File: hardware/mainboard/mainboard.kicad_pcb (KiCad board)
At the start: 4 copper layers, 28 x 110 mm, 45 parts, among them J1 Power Connector, J2 IN1, J3 IN2, J4 IN3, J5 INV OUT, J6 OUT, J7 CLIP OUT, U1 TL074

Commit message: Clean up
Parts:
- moved D3 9.90 mm to (53.9, 130.8)
- moved D4 9.32 mm to (53.9, 142.2)
- moved C4 9.24 mm to (66.5, 137.4), turned to -90 degrees
- moved R2 8.64 mm to (53.9, 139.8)
- moved R1 8.55 mm to (53.9, 133.2)
- moved C3 6.18 mm to (66.5, 133.2), turned to -90 degrees
- moved C1 4.93 mm to (60.2, 131.0), turned to -90 degrees
- moved C2 4.90 mm to (60.2, 141.2), turned to -90 degrees
- moved D1 4.37 mm to (66.5, 129.0), turned to 90 degrees
- moved D2 3.98 mm to (66.5, 142.7), turned to 90 degrees
- moved R11 1.91 mm to (74.9, 154.7), turned to 0 degrees
- moved R9 1.80 mm to (53.3, 154.7), turned to 180 degrees
- moved J1 1.70 mm to (71.5, 138.5)
- moved R10 1.64 mm to (63.0, 154.7), turned to 180 degrees
- moved C5 1.36 mm to (58.9, 102.4), turned to -90 degrees
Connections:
- net Net-(D5-A) renamed CLIP_DIODES
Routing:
- net -12V: track 75.6 -> 65.1 mm, vias 3 -> 4
- net Net-(D1-A): track 14.8 -> 7.81 mm, vias 1 -> 0
- net GND: track 3.32 -> 6.08 mm, vias 13 -> 15
- net Net-(J7-PadT): track 1.86 -> 4.33 mm
- net Net-(J5-PadT): track 1.86 -> 4.26 mm
- net Net-(J6-PadT): track 1.82 -> 4.12 mm
- net OUT: track 72.4 -> 70.5 mm
- net Net-(D2-K): track 11.6 -> 9.95 mm, vias 1 -> 0
- net CLIP_OUT: track 71.3 -> 69.9 mm, vias 2 -> 1
- net +12V: track 66.4 -> 66.8 mm, vias 2 -> 4
- net INV_OUT: track 77.3 -> 77.4 mm, vias 3 -> 4

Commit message: Cleanup
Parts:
- moved C3 2.20 mm to (66.3, 131.1)
- moved C4 2.07 mm to (66.3, 135.3)
- moved D1 2.01 mm to (66.3, 127.0)
- moved D2 1.22 mm to (66.3, 141.5)
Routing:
- net +12V: track 66.8 -> 64.2 mm
- net Net-(D1-A): track 7.81 -> 8.73 mm
- net GND: vias 15 -> 13
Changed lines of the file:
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@@
 	(footprint "Diode_SMD:D_SOD-323F"
 		(layer "B.Cu")
-		(at 66.5 129 90)
+		(at 66.3 127 90)
 		(descr "SOD-323F http://www.nxp.com/documents/outline_drawing/SOD323F.pdf")
 		(tags "SOD-323F")
@@
 	(footprint "Capacitor_SMD:C_0805_2012Metric_Pad1.18x1.45mm_HandSolder"
 		(layer "B.Cu")
-		(at 66.5 133.2375 -90)
+		(at 66.3 131.05125 -90)
 		(descr "Capacitor SMD 0805 (2012 Metric), square (rectangular) end terminal, IPC-7351 nominal with elongated pad for handsoldering. (Body size source: IPC-SM-782 page 76, https://www.pcb-3d.com/wordpress/wp-content/uploads/ipc-sm-782a_amendment_1_and_2.pdf, https://docs.google.com/spreadsheets/d/1BsfQQcO9C6DZCsRaXUlFlo91Tg2WpOkGARC1WS5S8t0/edit?usp=sharing), generated with kicad-footprint-generator")
 		(tags "capacitor handsolder")
@@
 	(footprint "Diode_SMD:D_SOD-323F"
 		(layer "B.Cu")
-		(at 66.5 142.7 90)
+		(at 66.3 141.5 90)
 		(descr "SOD-323F http://www.nxp.com/documents/outline_drawing/SOD323F.pdf")
 		(tags "SOD-323F")
@@
 	(footprint "Capacitor_SMD:C_0805_2012Metric_Pad1.18x1.45mm_HandSolder"
 		(layer "B.Cu")
-		(at 66.5 137.4 -90)
+		(at 66.3 135.3375 -90)
 		(descr "Capacitor SMD 0805 (2012 Metric), square (rectangular) end terminal, IPC-7351 nominal with elongated pad for handsoldering. (Body size source: IPC-SM-782 page 76, https://www.pcb-3d.com/wordpress/wp-content/uploads/ipc-sm-782a_amendment_1_and_2.pdf, https://docs.google.com/spreadsheets/d/1BsfQQcO9C6DZCsRaXUlFlo91Tg2WpOkGARC1WS5S8t0/edit?usp=sharing), generated with kicad-footprint-generator")
 		(tags "capacitor handsolder")
@@
 	)
 	(via
-		(at 66.5 136.3625)
-		(size 0.6)
-		(drill 0.3)
-		(layers "F.Cu" "B.Cu")
-		(net 1)
-	)
-	(via
 		(at 69.6 70.2)
 		(size 0.6)
@@
 	)
 	(via
-		(at 66.5 134.275)
-		(size 0.6)
-		(drill 0.3)
-		(layers "F.Cu" "B.Cu")
-		(net 1)
-	)
-	(via
 		(at 61.5 100.54)
 		(size 0.6)
@@
 	)
 	(segment
-		(start 60.25 128.25)
-		(end 62.55 128.25)
-		(width 0.3)
+		(start 65.201 109.723)
+		(end 65.201 100.701)
+		(width 0.2)
 		(layer "F.Cu")
 		(net 2)
 	)
 	(segment
-		(start 65.201 109.723)
-		(end 65.201 100.701)
+		(start 74 113.529009)
+		(end 74 113)
 		(width 0.2)
 		(layer "F.Cu")
@@
 	)
 	(segment
-		(start 74 113)
-		(end 74 114.5)
+		(start 66.3 130.01375)
+		(end 66.3 121.229009)
 		(width 0.2)
 		(layer "F.Cu")
@@
 	)
 	(segment
-		(start 74 114.5)
-		(end 60.2 128.3)
+		(start 60.2 128.3)
+		(end 64.58625 128.3)
+		(width 0.3)
+		(layer "F.Cu")
+		(net 2)
+	)
+	(segment
+		(start 66.3 121.229009)
+		(end 74 113.529009)
 		(width 0.2)
 		(layer "F.Cu")
@@
 	)
 	(segment
-		(start 62.55 128.25)
-		(end 66.5 132.2)
+		(start 64.58625 128.3)
+		(end 66.3 130.01375)
 		(width 0.3)
 		(layer "F.Cu")
@@
 	)
 	(via
-		(at 66.5 132.2)
+		(at 52.9 130.8)
 		(size 0.6)
 		(drill 0.3)
@@
 	)
 	(via
-		(at 52.9 130.8)
+		(at 64.75 100.25)
 		(size 0.6)
 		(drill 0.3)
@@
 	)
 	(via
-		(at 64.75 100.25)
+		(at 66.3 130.01375)
 		(size 0.6)
 		(drill 0.3)
@@
 	)
 	(segment
-		(start 66.5 130.1)
-		(end 66.5 132.2)
-		(width 0.3)
+		(start 63.19 101.81)
+		(end 61.5 101.81)
+		(width 0.2)
 		(layer "B.Cu")
 		(net 2)
 	)
 	(segment
-		(start 63.19 101.81)
-		(end 61.5 101.81)
+		(start 66.5 127.9)
+		(end 66.4 127.9)
 		(width 0.2)
 		(layer "B.Cu")
@@
 	)
 	(segment
-		(start 61.5 101.81)
-		(end 59.31 101.81)
+		(start 66.3 130.01375)
+		(end 66.3 128.1)
 		(width 0.2)
 		(layer "B.Cu")
@@
 	)
 	(segment
-		(start 66.4 132.2)
-		(end 65.949 131.749)
+		(start 61.5 101.81)
+		(end 59.31 101.81)
 		(width 0.2)
 		(layer "B.Cu")
@@
 	)
 	(segment
-		(start 67.101 137.8365)
-		(end 66.5 138.4375)
-		(width 0.2)
+		(start 69 125)
+		(end 74 120)
+		(width 0.3)
 		(layer "F.Cu")
 		(net 3)
 	)
 	(segment
-		(start 74 120)
-		(end 67.101 126.899)
-		(width 0.2)
+		(start 66.3 136.375)
+		(end 69 133.675)
+		(width 0.3)
+		(layer "F.Cu")
+		(net 3)
+	)
+	(segment
+		(start 60.25 143.95)
+		(end 66.3 137.9)
+		(width 0.3)
 		(layer "F.Cu")
 		(net 3)
 	)
 	(segment
-		(start 65.7625 138.4375)
-		(end 66.5 138.4375)
+		(start 69 133.675)
+		(end 69 125)
 		(width 0.3)
 		(layer "F.Cu")
@@
 	)
 	(segment
-		(start 67.101 126.899)
-		(end 67.101 137.8365)
-		(width 0.2)
+		(start 66.3 137.9)
+		(end 66.3 136.375)
+		(width 0.3)
 		(layer "F.Cu")
 		(net 3)
@@
 		(net 3)
 	)
-	(segment
-		(start 60.25 143.95)
-		(end 65.7625 138.4375)
-		(width 0.3)
-		(layer "F.Cu")
-		(net 3)
-	)
 	(via
-		(at 66.5 138.4375)
+		(at 55 142.2)
 		(size 0.6)
 		(drill 0.3)
@@
 	)
 	(via
-		(at 55 142.2)
+		(at 60.25 143.95)
 		(size 0.6)
 		(drill 0.3)
@@
 	)
 	(via
-		(at 60.25 143.95)
+		(at 66.3 136.375)
 		(size 0.6)
 		(drill 0.3)
@@
 	)
 	(segment
-		(start 66.3 138.4375)
-		(end 65.949 138.7885)
-		(width 0.2)
-		(layer "B.Cu")
-		(net 3)
-	)
-	(segment
-		(start 66.5 141.6)
-		(end 66.5 138.4375)
-		(width 0.3)
-		(layer "B.Cu")
-		(net 3)
-	)
-	(segment
 		(start 72.25 106.5)
 		(end 72.25 105.25)
@@
 	)
 	(segment
-		(start 66.5 127.9)
-		(end 66.4 127.9)
-		(width 0.2)
+		(start 66.3 136.375)
+		(end 66.3 140.4)
+		(width 0.3)
 		(layer "B.Cu")
-		(net 4)
+		(net 3)
 	)
 	(segment
-		(start 71.5 128.3)
-		(end 66.9 128.3)
-		(width 0.3)
+		(start 66.3 125.9)
+		(end 69.1 125.9)
+		(width 0.2)
 		(layer "B.Cu")
 		(net 4)
 	)
 	(segment
-		(start 66.9 128.3)
-		(end 66.5 127.9)
-		(width 0.3)
+		(start 69.1 125.9)
+		(end 71.5 128.3)
+		(width 0.2)
 		(layer "B.Cu")
 		(net 4)
@@
 	)
 	(segment
-		(start 71.5 138.8)
-		(end 66.5 143.8)
+		(start 66.3 142.6)
+		(end 67.36 142.6)
 		(width 0.3)
 		(layer "B.Cu")
@@
 	)
 	(segment
+		(start 67.36 142.6)
+		(end 71.5 138.46)
+		(width 0.3)
+		(layer "B.Cu")
+		(net 5)
+	)
+	(segment
 		(start 71.5 138.46)
 		(end 71.5 138.8)
@@
 		(min_thickness 0.25)
 		(filled_areas_thickness no)
-		(fill
+		(fill yes
 			(thermal_gap 0.5)
 			(thermal_bridge_width 0.5)
@@
 		(min_thickness 0.25)
 		(filled_areas_thickness no)
-		(fill
+		(fill yes
 			(thermal_gap 0.5)
 			(thermal_bridge_width 0.5)
@@
 		(min_thickness 0.25)
 		(filled_areas_thickness no)
-		(fill
+		(fill yes
 			(thermal_gap 0.5)
 			(thermal_bridge_width 0.5)
@@
 		(min_thickness 0.25)
 		(filled_areas_thickness no)
-		(fill
+		(fill yes
 			(thermal_gap 0.5)
 			(thermal_bridge_width 0.5)

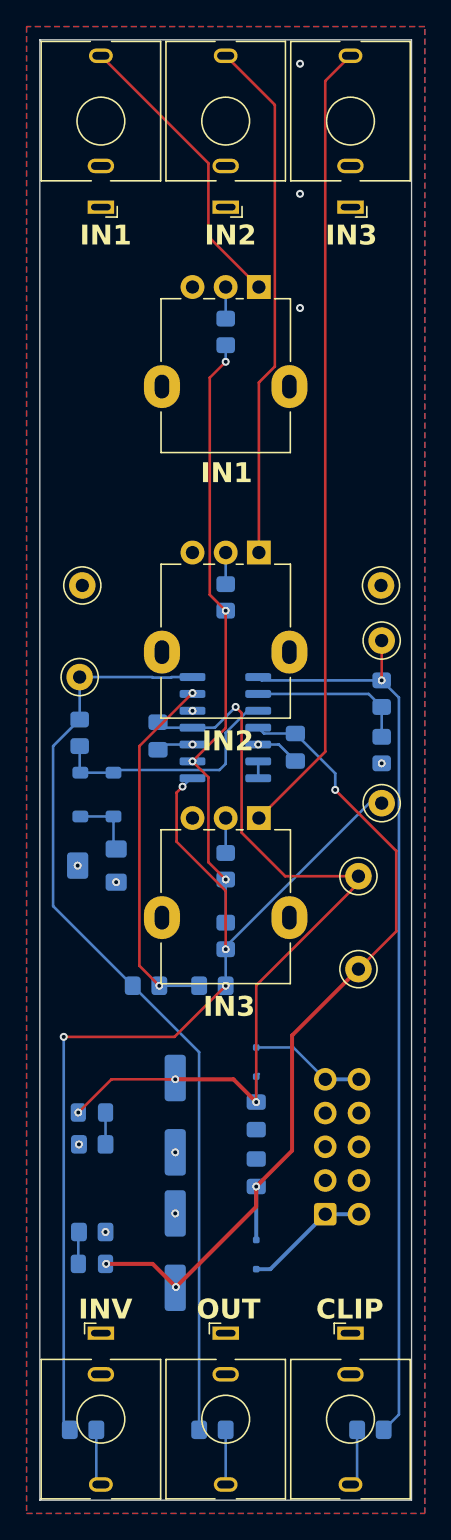
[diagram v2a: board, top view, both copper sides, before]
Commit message: Add 10Ω resistors to power rails
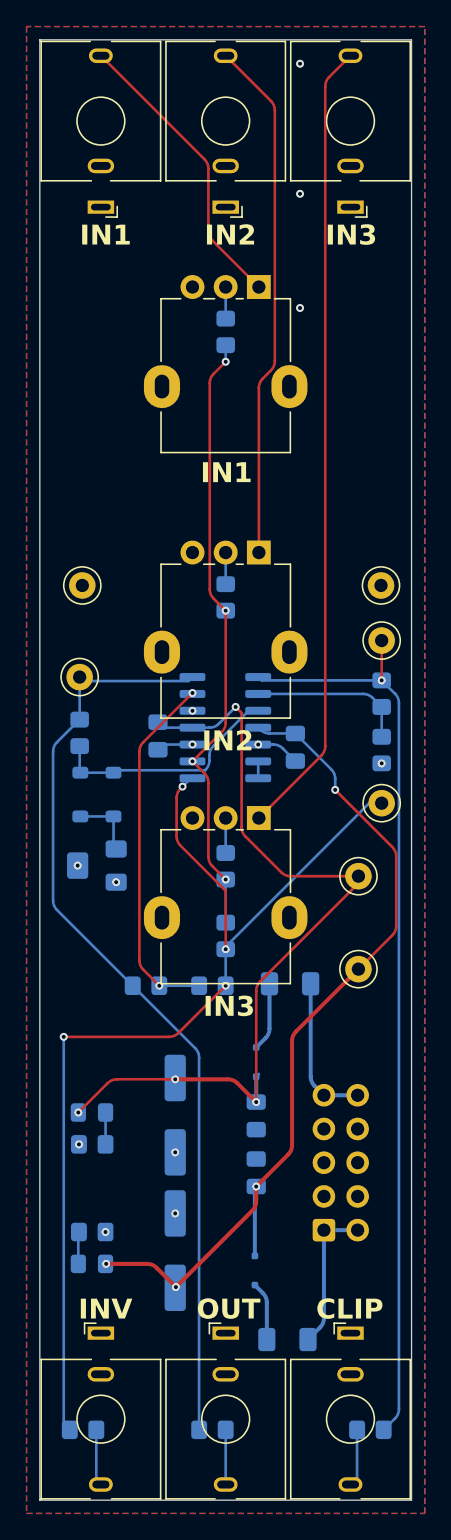
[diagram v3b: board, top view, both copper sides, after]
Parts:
- added R14: 10Ω, Resistor_SMD:R_1206_3216Metric_Pad1.30x1.75mm_HandSolder, B.Cu at (68.8, 121.1)
- added R16: 10Ω, Resistor_SMD:R_1206_3216Metric_Pad1.30x1.75mm_HandSolder, B.Cu at (68.7, 147.9)
- moved D2 1.20 mm to (66.2, 142.7)
- moved J1 1.20 mm to (71.4, 139.7)
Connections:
- J1 pad 1: Net-(D2-K) -> Net-(J1-Pin_1)
- J1 pad 10: Net-(D1-A) -> Net-(J1-Pin_10)
- J1 pad 2: Net-(D2-K) -> Net-(J1-Pin_1)
- J1 pad 9: Net-(D1-A) -> Net-(J1-Pin_10)
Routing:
- net Net-(J1-Pin_10): track 0.00 -> 11.3 mm
- net Net-(J1-Pin_1): track 0.00 -> 11.2 mm
- net Net-(D2-K): track 9.79 -> 4.42 mm
- net Net-(D1-A): track 8.73 -> 5.17 mm
- net -12V: track 65.0 -> 65.9 mm

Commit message: Updates
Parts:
- D1, D2: footprint Diode_SMD:D_SOD-323F -> EurorackFootprints:D_SOD-323F
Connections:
- RV1 pad 1: Net-(J2-PadT) -> GND
- RV1 pad 3: GND -> Net-(J2-PadT)
- RV2 pad 1: Net-(J3-PadT) -> GND
- RV2 pad 3: GND -> Net-(J3-PadT)
- RV3 pad 1: Net-(J4-PadT) -> GND
- RV3 pad 3: GND -> Net-(J4-PadT)
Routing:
- net Net-(J4-PadT): track 60.2 -> 66.6 mm, vias 0 -> 1
- net Net-(J2-PadT): track 22.3 -> 20.3 mm
- net OUT: track 70.5 -> 71.9 mm
- net Net-(J3-PadT): track 39.3 -> 38.7 mm
- net GND: vias 13 -> 17
- net CLIP_OUT: vias 1 -> 0
